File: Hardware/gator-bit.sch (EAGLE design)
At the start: 89 parts, among them J1 GATOR, J19 GATOR, J2 GATOR, J20 GATOR, J21 GATOR, J22 GATOR, J25 GATOR, J28 GATOR, J3 GATOR, J32 GATOR, J33 GATOR, J34 GATOR, J35 GATOR, J36 GATOR, J39 GATOR, J4 GATOR, J40 GATOR, U1 TPS63070, U2 micro:bit, U4 V_REG_MIC52053.0V, U6 GATORBIT_LM317

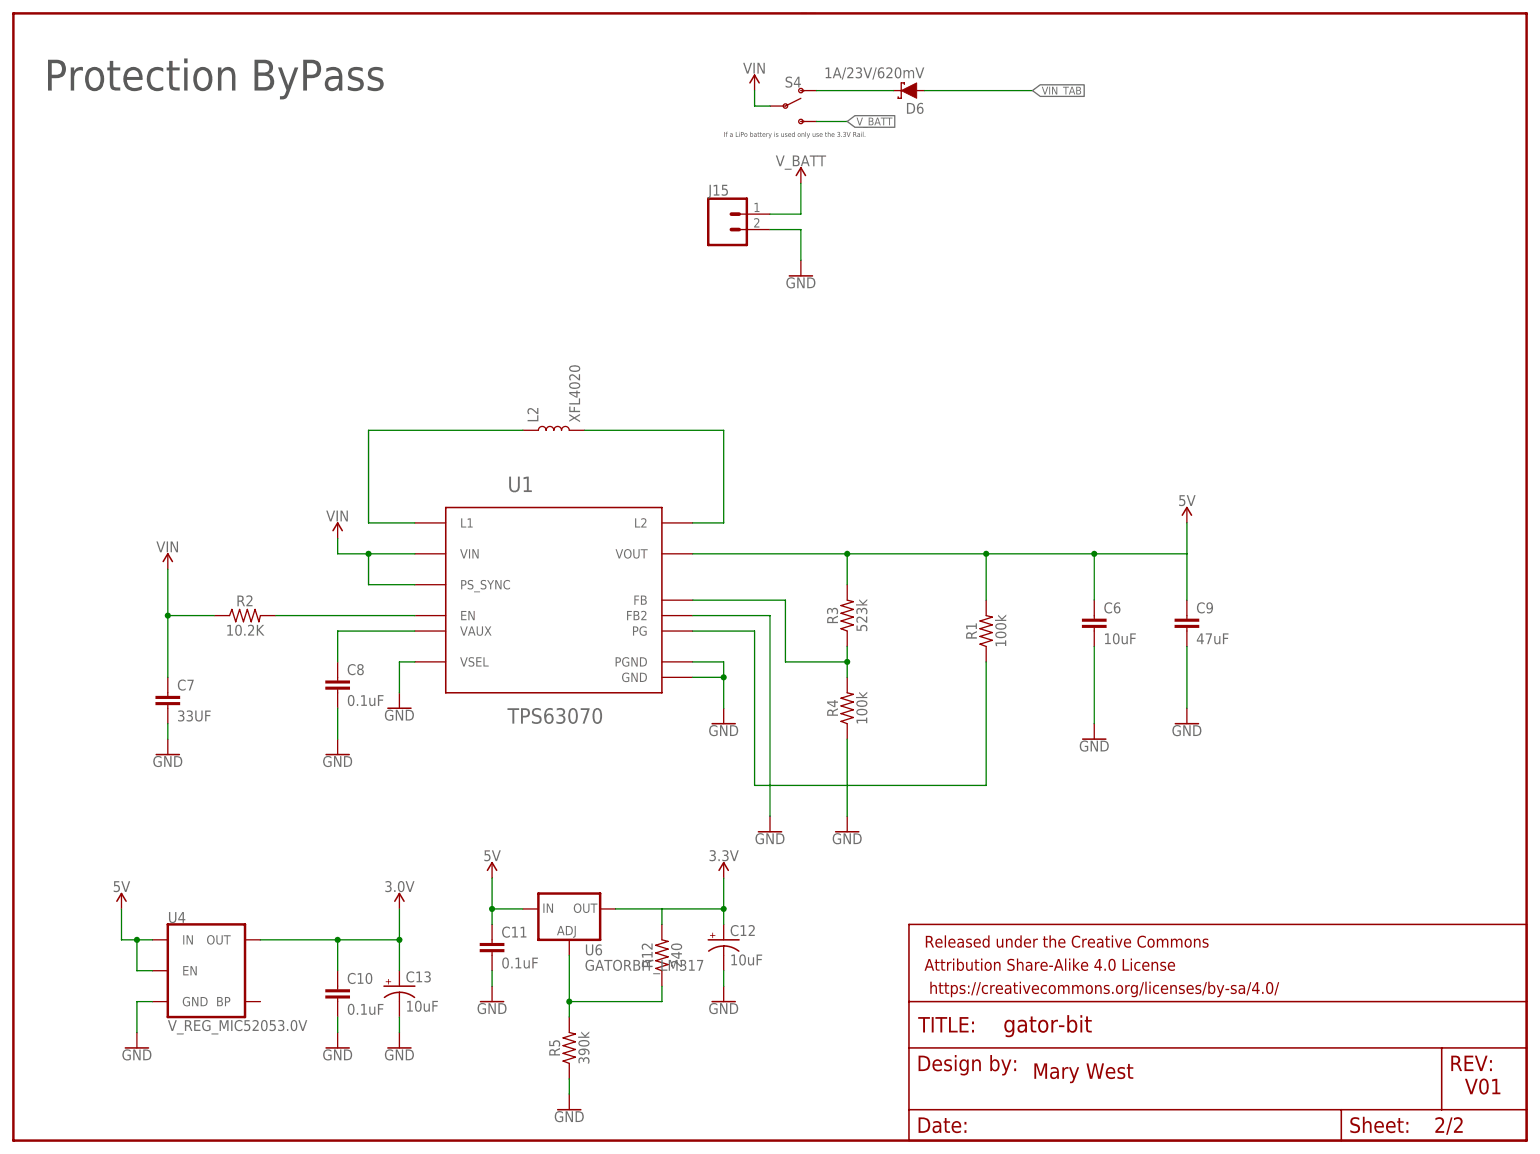
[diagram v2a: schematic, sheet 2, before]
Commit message: added holes for lego compatibility
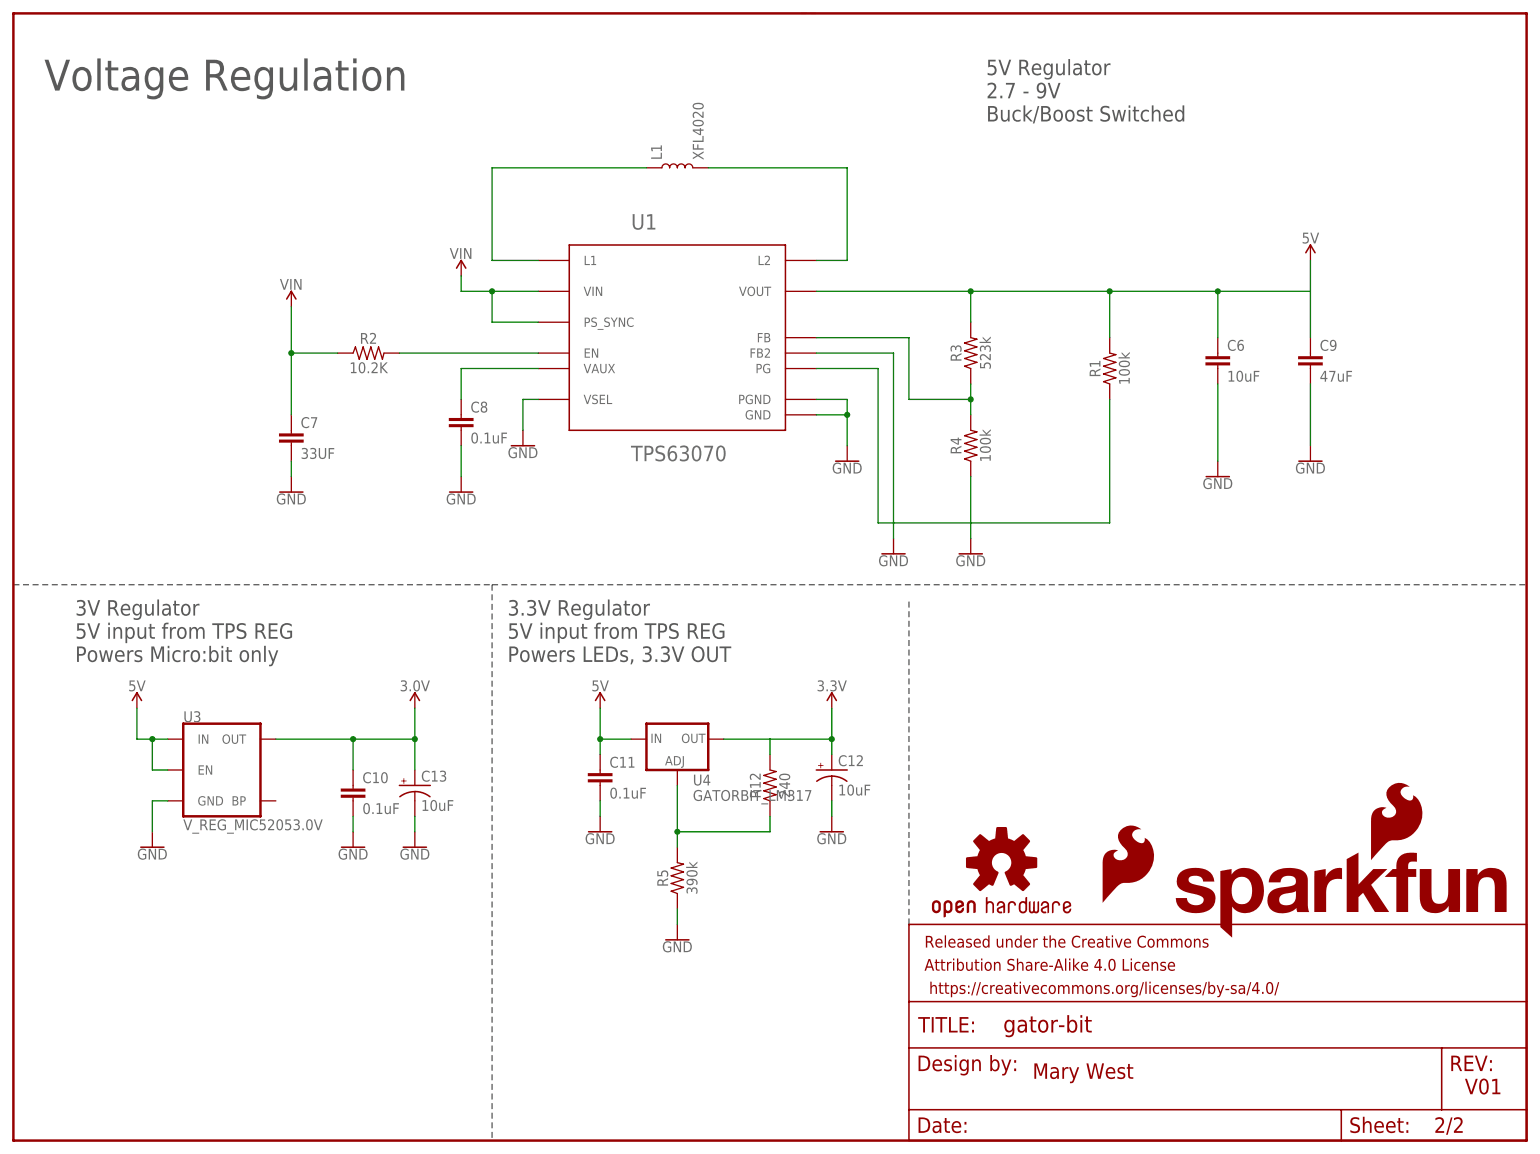
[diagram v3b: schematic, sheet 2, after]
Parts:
- removed D21, D23, D24, D25: 3.3V, SparkFun-DiscreteSemi:DIODE-ZENER-MM3Z3V3T1G
- removed J35: GATOR, TAB:GATOR
- removed L2: XFL4020, SparkFun-Coils:XFL4020
- removed LOGO1: SFE_LOGO_FLAME.3_INCH, SparkFun-Aesthetics:SFE_LOGO_FLAME.3_INCH
- removed LOGO2: OSHW-LOGOL, SparkFun-Aesthetics:OSHW-LOGOL
- removed LOGO3: SFE_LOGO_NAME_FLAME.3_INCH, SparkFun-Aesthetics:SFE_LOGO_NAME_FLAME.3_INCH
- removed S4: (no value), SparkFun-Switches:SWITCH-SPDT-SMD-AYZ0202
- removed U6: GATORBIT_LM317, SparkFun-IC-Power:GATORBIT_LM317
- added 13, D10, D7, D8: 3.3V, SparkFun-DiscreteSemi:DIODE-ZENER-MM3Z3V3T1G
- added J5: (no value), SparkFun-Connectors:CONN_02-JST-2MM-SMT
- added L1: XFL4020, SparkFun-Coils:XFL4020
- added LOGO4: SFE_LOGO_NAME_FLAME.3_INCH, SparkFun-Aesthetics:SFE_LOGO_NAME_FLAME.3_INCH
- added LOGO5: SFE_LOGO_FLAME.3_INCH, SparkFun-Aesthetics:SFE_LOGO_FLAME.3_INCH
- added LOGO6: OSHW-LOGOL, SparkFun-Aesthetics:OSHW-LOGOL
- added S2: (no value), SparkFun-Switches:SWITCH-SPDT-SMD-AYZ0202
- added U3: V_REG_MIC52053.0V, SparkFun-IC-Power:V_REG_MIC52053.0V
- J15: value (none) -> GATOR; device SparkFun-Connectors:CONN_02-JST-2MM-SMT -> TAB:GATOR
- U4: value V_REG_MIC52053.0V -> GATORBIT_LM317; device SparkFun-IC-Power:V_REG_MIC52053.0V -> SparkFun-IC-Power:GATORBIT_LM317
- renumbered D13 to D9, D22 to D17, J19 to J6, J20 to J7, J21 to J8, J22 to J9, J25 to J10, J28 to J11, J32 to J12, J33 to J13, J34 to J14, J36 to J16, J39 to J17, J40 to J18
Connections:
- removed net N$9: D6.C, S4.O
- new net N$20: D6.C, S2.O
- net 3.0V: now also D14.C, D16.C, D18.C, D20.C, D7.C, U3.OUT; no longer D15.C, D19.C, D21.C, D23.C, D25.C, U4.OUT
- net 3.3V: now also U4.OUT; no longer U6.OUT
- net 5V: now also U3.EN, U3.IN; no longer U4.EN, U6.IN
- net GND: now also 13.A, D10.A, D15.A, D19.A, D8.A, J5.1, U3.GND; no longer D14.A, D16.A, D18.A, D20.A, D24.A, J15.1, U4.GND
- net N$16: now also U4.ADJ; no longer U6.ADJ
- net N$2: now also L1.1; no longer L2.1
- net N$8: now also L1.2; no longer L2.2
- net P16+: now also J15.P$1; no longer J35.P$1
- net PP0: now also D12.C, D14.A; no longer D16.C, D19.A
- net PP1: now also D15.C, D16.A; no longer D20.C, D21.A
- net PP11: now also D10.C, D11.A; no longer D14.C, D15.A
- net PP16: now also 13.C, D7.A; no longer D11.A, D18.C
- net PP2: now also D18.A; no longer D23.A
- net PP5: now also D19.C, D20.A; no longer D24.C, D25.A
- net PP8: now also D8.C; no longer D12.C
- net VIN: now also S2.P; no longer S4.P
- net V_BATT: now also J5.2, S2.S; no longer J15.2, S4.S
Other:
- note added: "3.3V Regulator 5V input from TPS REG Powers LEDs, 3.3V OUT"
- note added: "3V Regulator 5V input from TPS REG Powers Micro:bit only"
- note added: "5V Regulator 2.7 - 9V Buck/Boost Switched"
- note added: "Alligator Clip Terminals"
- note added: "Battery or external supply"
- note added: "IO Protection"
- note added: "To use speaker Pin0 can not be used anymore"
- note added: "Turn on regulated output"
- note added: "Voltage Regulation"
- note removed: "Clips"
- note removed: "If a LiPo battery is used only use the 3.3V Rail."
- note removed: "Protection"
- note removed: "Protection ByPass"
- moved on the sheet: C10, C11, C12, C13, C6, C7, C8, C9, D11, D12, D14, D15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

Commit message: Updated parts with SKUs
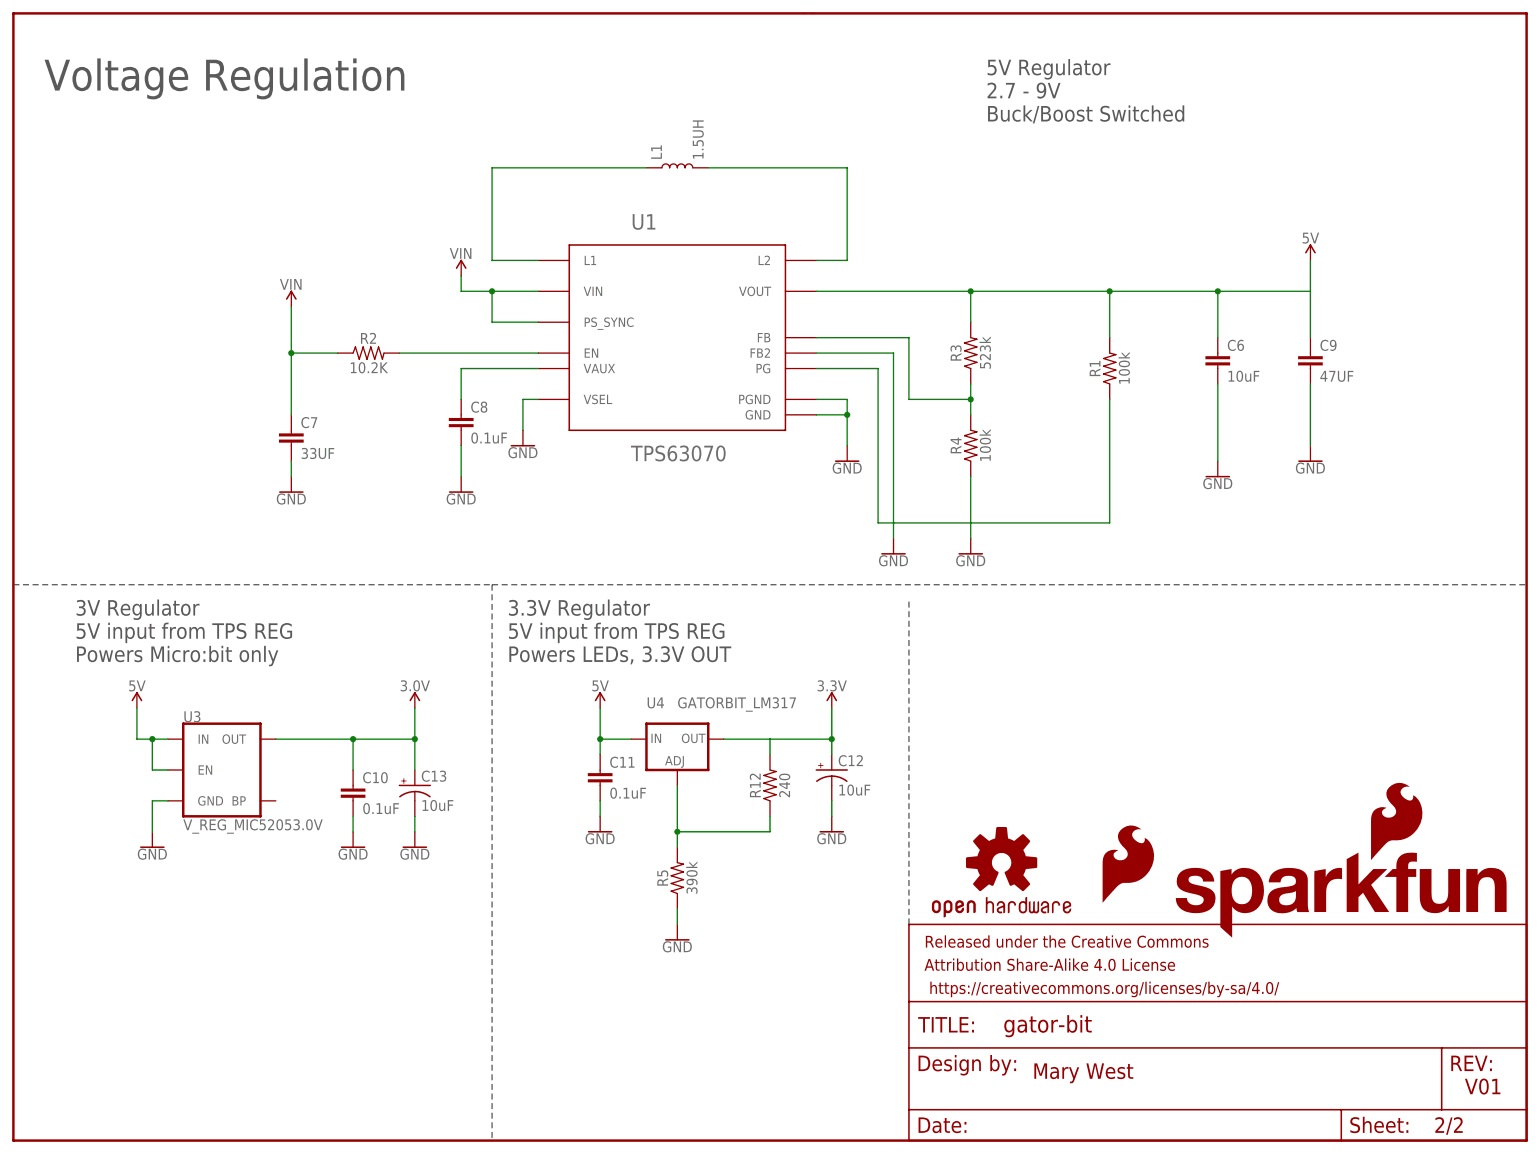
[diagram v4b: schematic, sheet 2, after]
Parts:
- C9: value 47uF -> 47UF
- L1: value XFL4020 -> 1.5UH
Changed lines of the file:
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@@
 <part name="C7" library="SparkFun-Capacitors" deviceset="33UF" device="" technology="20%-6.3V-0805" value="33UF"/>
 <part name="C8" library="SparkFun-Capacitors" deviceset="0.1UF" device="-0603-25V-(+80/-20%)" value="0.1uF"/>
-<part name="C9" library="SparkFun-Capacitors" deviceset="47UF" device="" technology="20%-6.3V-0805" value="47uF"/>
-<part name="L1" library="SparkFun-Coils" deviceset="XFL4020" device=""/>
+<part name="C9" library="SparkFun-Capacitors" deviceset="47UF" device="" technology="20%-6.3V-0805" value="47UF"/>
+<part name="L1" library="SparkFun-Coils" deviceset="XFL4020" device="" value="1.5UH"/>
 <part name="GND7" library="SparkFun-PowerSymbols" deviceset="GND" device=""/>
 <part name="GND8" library="SparkFun-PowerSymbols" deviceset="GND" device=""/>
@@
 <instance part="SUPPLY26" gate="G$1" x="66.04" y="71.12"/>
 <instance part="SUPPLY27" gate="G$1" x="134.62" y="71.12"/>
-<instance part="U4" gate="G$1" x="109.22" y="66.04"/>
+<instance part="U4" gate="G$1" x="109.22" y="66.04" smashed="yes">
+<attribute name="NAME" x="104.14" y="71.12" size="1.778" layer="95"/>
+<attribute name="VALUE" x="109.22" y="71.12" size="1.778" layer="96"/>
+</instance>
 <instance part="R5" gate="G$1" x="109.22" y="43.18" rot="R90"/>
 <instance part="R12" gate="G$1" x="124.46" y="58.42" rot="R90"/>

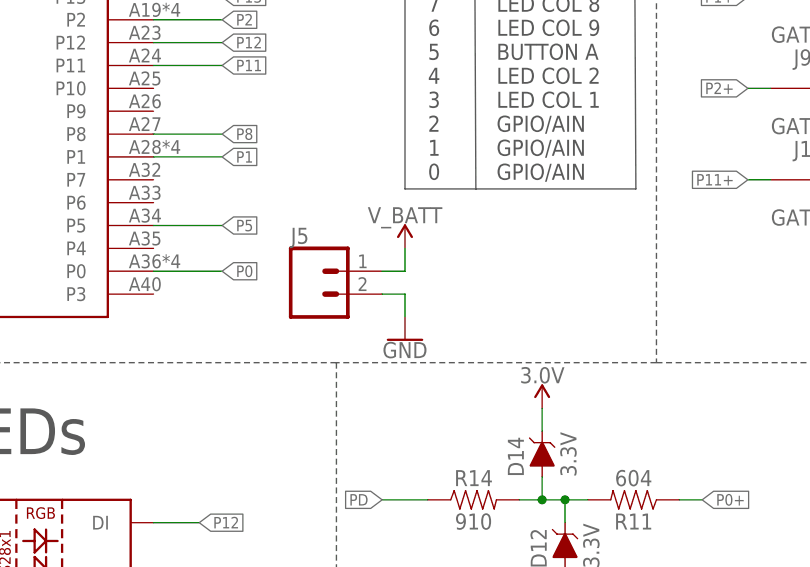
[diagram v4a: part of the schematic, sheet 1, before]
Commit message: updating Buck-Boost part
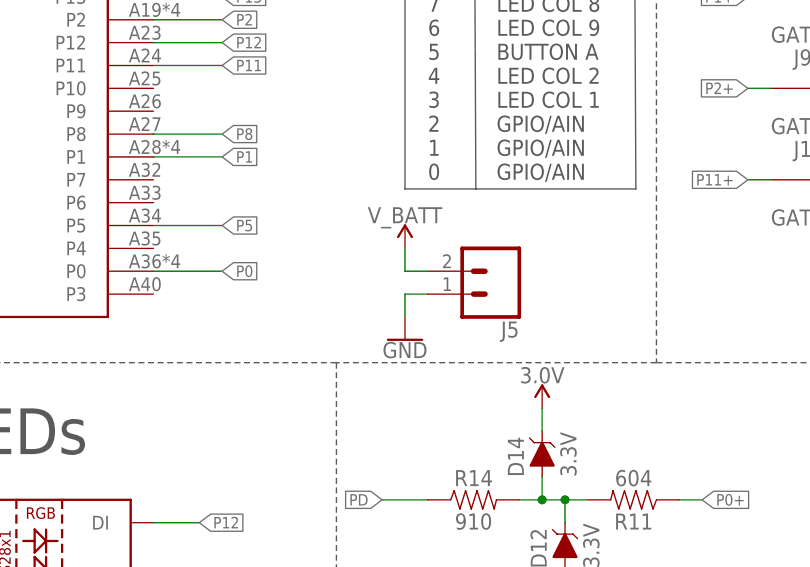
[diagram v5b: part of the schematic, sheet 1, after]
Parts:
- U4: value GATORBIT_LM317 -> ADJ REG 1.5A
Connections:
- net GND: now also J5.2; no longer J5.1
- net V_BATT: now also J5.1; no longer J5.2
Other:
- moved on the sheet: J5
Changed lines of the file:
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@@
 <part name="SUPPLY27" library="SparkFun-PowerSymbols" deviceset="3.3V" device=""/>
 <part name="FD3" library="SparkFun-Aesthetics" deviceset="FIDUCIAL" device="1X2"/>
-<part name="U4" library="SparkFun-IC-Power" deviceset="GATORBIT_LM317" device=""/>
+<part name="U4" library="SparkFun-IC-Power" deviceset="GATORBIT_LM317" device="" value="ADJ REG 1.5A"/>
 <part name="R5" library="SparkFun-Resistors" deviceset="390KOHM" device="-0603-1/10W-1%" value="390k"/>
 <part name="R12" library="SparkFun-Resistors" deviceset="240OHM" device="-0603-1/10W-1%" value="240"/>
@@
 <instance part="SUPPLY25" gate="G$1" x="243.84" y="119.38"/>
 <instance part="FD3" gate="G$1" x="238.76" y="33.02"/>
-<instance part="J5" gate="G$1" x="63.5" y="116.84"/>
+<instance part="J5" gate="G$1" x="83.82" y="119.38" rot="R180"/>
 <instance part="GND29" gate="1" x="73.66" y="111.76"/>
 <instance part="SUPPLY28" gate="G$1" x="73.66" y="121.92"/>
@@
 </segment>
 <segment>
-<pinref part="J5" gate="G$1" pin="1"/>
-<wire x1="71.12" y1="116.84" x2="73.66" y2="116.84" width="0.1524" layer="91"/>
+<pinref part="J5" gate="G$1" pin="2"/>
+<wire x1="76.2" y1="116.84" x2="73.66" y2="116.84" width="0.1524" layer="91"/>
+<pinref part="GND29" gate="1" pin="GND"/>
 <wire x1="73.66" y1="116.84" x2="73.66" y2="114.3" width="0.1524" layer="91"/>
-<pinref part="GND29" gate="1" pin="GND"/>
 </segment>
 </net>
@@
 <net name="V_BATT" class="0">
 <segment>
-<pinref part="J5" gate="G$1" pin="2"/>
-<wire x1="71.12" y1="119.38" x2="73.66" y2="119.38" width="0.1524" layer="91"/>
-<wire x1="73.66" y1="119.38" x2="73.66" y2="121.92" width="0.1524" layer="91"/>
-<pinref part="SUPPLY28" gate="G$1" pin="V_BATT"/>
-</segment>
-<segment>
 <pinref part="S2" gate="1" pin="S"/>
 <wire x1="213.36" y1="139.7" x2="218.44" y2="139.7" width="0.1524" layer="91"/>
 <label x="218.44" y="139.7" size="1.27" layer="95" xref="yes"/>
 </segment>
-</net>
+<segment>
+<pinref part="J5" gate="G$1" pin="1"/>
+<wire x1="76.2" y1="119.38" x2="73.66" y2="119.38" width="0.1524" layer="91"/>
+<pinref part="SUPPLY28" gate="G$1" pin="V_BATT"/>
+<wire x1="73.66" y1="119.38" x2="73.66" y2="121.92" width="0.1524" layer="91"/>
+</segment>
+</net>
